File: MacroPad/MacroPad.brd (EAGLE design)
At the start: 120.6 x 68.2 mm, 69 parts, among them IC1 MIC5219BM5, J1 USB4085-GF-A_REVA4, U1 ATMEGA32U4-AUR, Y1 XRCGB16M000FXN00R0

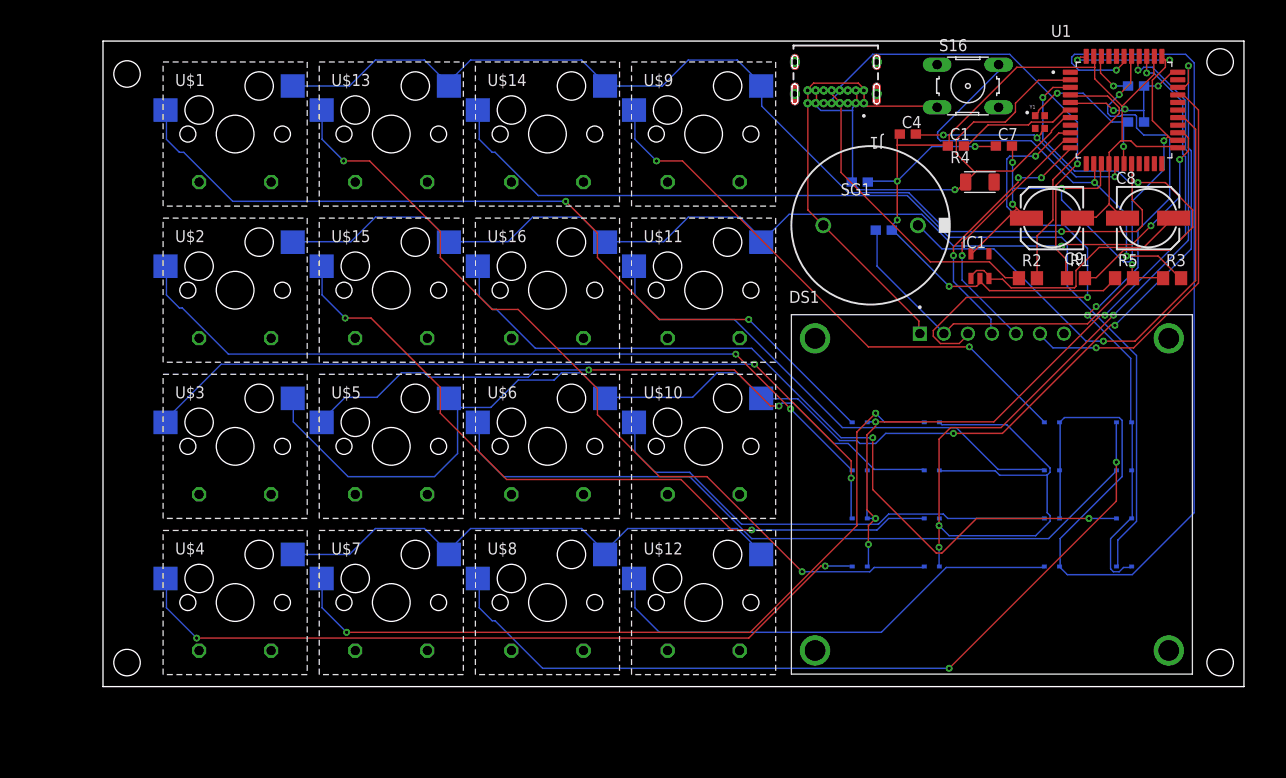
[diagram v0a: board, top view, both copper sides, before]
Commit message: Fixed some DRC errors
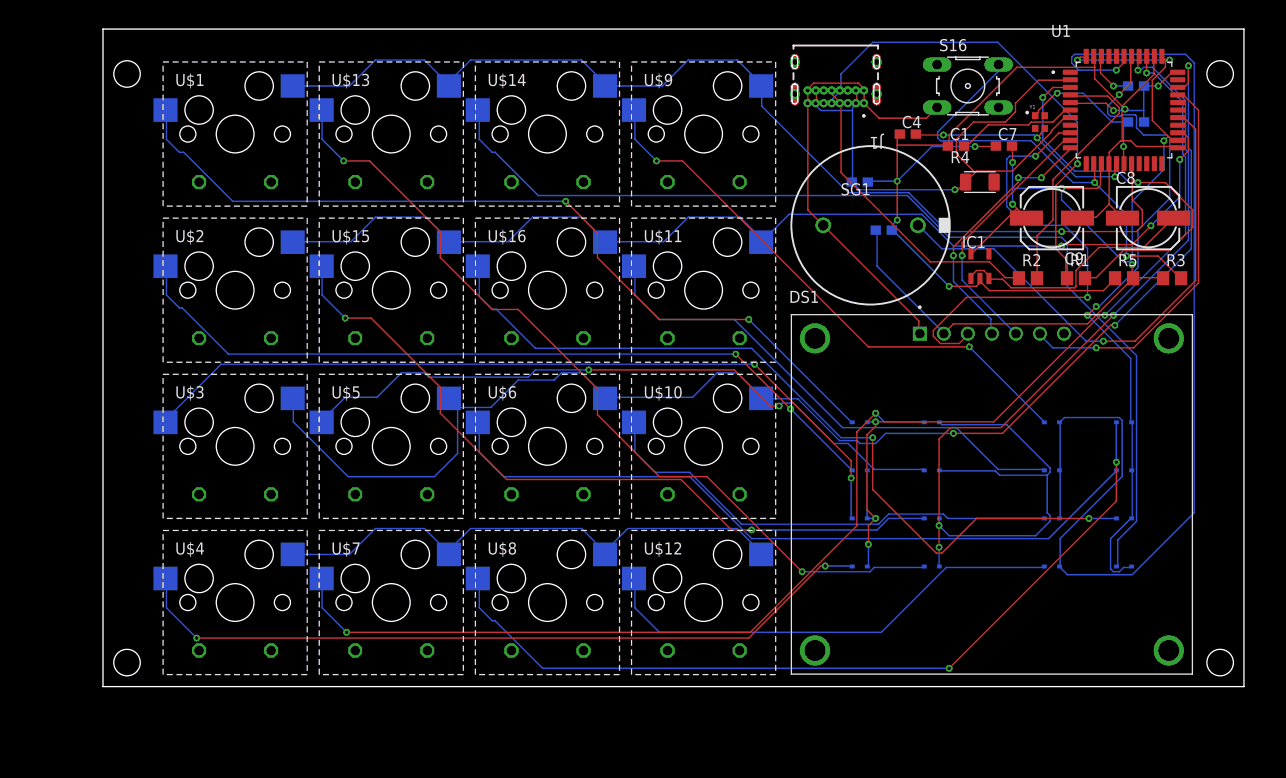
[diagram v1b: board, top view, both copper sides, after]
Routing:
- net N$20: track 49.6 -> 51.4 mm
- net DGND: track 46.8 -> 47.7 mm
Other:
- board size 120.6 x 68.2 mm -> 120.6 x 69.5 mm
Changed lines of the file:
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@@
 <drawing>
 <settings>
-<setting alwaysvectorfont="no"/>
+<setting alwaysvectorfont="yes"/>
 <setting verticaltext="up"/>
 </settings>
@@
 <plain>
 <wire x1="0" y1="0" x2="120.63" y2="0" width="0" layer="20"/>
-<wire x1="120.63" y1="0" x2="120.63" y2="68.25" width="0" layer="20"/>
-<wire x1="120.63" y1="68.25" x2="0" y2="68.25" width="0" layer="20"/>
-<wire x1="0" y1="68.25" x2="0" y2="0" width="0" layer="20"/>
+<wire x1="120.63" y1="0" x2="120.63" y2="69.52" width="0" layer="20"/>
+<wire x1="120.63" y1="69.52" x2="0" y2="69.52" width="0" layer="20"/>
+<wire x1="0" y1="69.52" x2="0" y2="0" width="0" layer="20"/>
 <hole x="2.54" y="64.77" drill="2.8"/>
 <hole x="2.54" y="2.54" drill="2.8"/>
-<hole x="118.11" y="66.04" drill="2.8"/>
+<hole x="118.11" y="64.77" drill="2.8"/>
 <hole x="118.11" y="2.54" drill="2.8"/>
 <text x="2.54" y="6.35" size="1.778" layer="45" rot="R90">Dyl's Macropad</text>
-<text x="119.38" y="21.59" size="1.778" layer="45" rot="R90">If you're reading this: have a nice day!</text>
+<text x="119.38" y="20.32" size="1.778" layer="45" rot="R90">If you're reading this: have a nice day!</text>
 </plain>
 <attributes>
@@
 <wire x1="74.5236" y1="63.0428" x2="74.495" y2="63.03" width="0.1524" layer="1"/>
 <wire x1="80.3148" y1="63.0428" x2="80.445" y2="63.03" width="0.1524" layer="1"/>
-<wire x1="80.772" y1="61.3664" x2="88.0872" y2="61.3664" width="0.1524" layer="1"/>
-<wire x1="80.4672" y1="61.6712" x2="80.772" y2="61.3664" width="0.1524" layer="1"/>
-<wire x1="88.0872" y1="61.3664" x2="88.1888" y2="61.2394" width="0.1524" layer="1"/>
+<wire x1="88.1888" y1="61.2394" x2="87.0458" y2="60.0964" width="0.1524" layer="1"/>
+<wire x1="87.0458" y1="60.0964" x2="82.042" y2="60.0964" width="0.1524" layer="1"/>
+<wire x1="80.4672" y1="61.6712" x2="82.042" y2="60.0964" width="0.1524" layer="1"/>
 <wire x1="80.4672" y1="61.6712" x2="80.445" y2="61.68" width="0.1524" layer="1"/>
 <wire x1="86.2584" y1="38.6588" x2="86.2584" y2="37.4396" width="0.1524" layer="1"/>
@@
 <wire x1="103.0224" y1="55.2704" x2="100.7364" y2="52.9844" width="0.1524" layer="1"/>
 <wire x1="103.0224" y1="59.69" x2="103.0224" y2="55.2704" width="0.1524" layer="16"/>
-<wire x1="95.8596" y1="66.8528" x2="103.0224" y2="59.69" width="0.1524" layer="16"/>
-<wire x1="81.3816" y1="66.8528" x2="95.8596" y2="66.8528" width="0.1524" layer="16"/>
-<wire x1="78.0288" y1="63.5" x2="81.3816" y2="66.8528" width="0.1524" layer="16"/>
-<wire x1="78.0288" y1="63.0428" x2="78.0288" y2="63.5" width="0.1524" layer="16"/>
+<wire x1="94.5896" y1="68.1228" x2="103.0224" y2="59.69" width="0.1524" layer="16"/>
+<wire x1="81.3816" y1="68.1228" x2="94.5896" y2="68.1228" width="0.1524" layer="16"/>
+<wire x1="78.0288" y1="64.77" x2="81.3816" y2="68.1228" width="0.1524" layer="16"/>
+<wire x1="78.0288" y1="63.0428" x2="78.0288" y2="64.77" width="0.1524" layer="16"/>
 <wire x1="101.8032" y1="43.2308" x2="101.92" y2="43.18" width="0.1524" layer="1"/>
 <wire x1="78.0288" y1="63.0428" x2="77.895" y2="63.03" width="0.1524" layer="16"/>

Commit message: Problematic DRC issues cleared
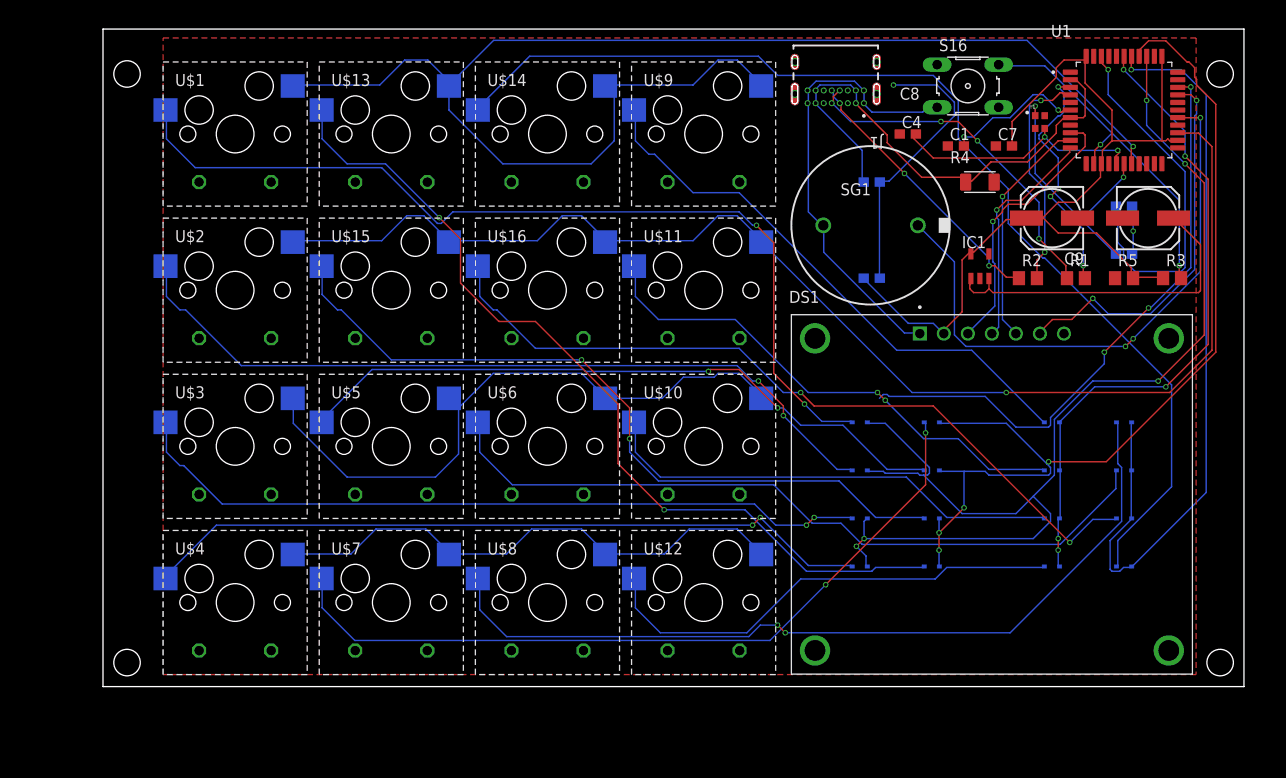
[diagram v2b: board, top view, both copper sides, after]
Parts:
- moved C5 14.0 mm to (108.0, 45.7)
- moved C2 12.8 mm to (108.0, 50.8)
- moved C6 5.24 mm to (81.3, 43.2)
- moved C3 1.27 mm to (81.3, 53.3)
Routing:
- net GND: track 131.7 -> 34.9 mm, vias 7 -> 2
- net A3: track 121.2 -> 68.8 mm, vias 1 -> 5
- net D3: track 112.5 -> 149.4 mm
- net A0: track 85.3 -> 120.6 mm
- net N$23: track 5.28 -> 39.3 mm
- net D4: track 113.8 -> 138.7 mm, vias 3 -> 1
- net D15: track 51.3 -> 29.1 mm, vias 2 -> 1
- net DN: track 42.2 -> 25.7 mm, vias 2 -> 4
- net VCC: track 116.9 -> 100.6 mm, vias 7 -> 0
- net A1: track 116.4 -> 100.9 mm
- net D5: track 146.6 -> 132.0 mm
- net N$20: track 51.4 -> 37.2 mm, vias 1 -> 3
- net A2: track 70.5 -> 82.7 mm, vias 3 -> 1
- net XTAL1: track 16.6 -> 28.0 mm
- net RST: track 47.0 -> 37.5 mm
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- added copper zone on layer 1, net GND

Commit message: Added missing diode
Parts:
- added D17: 1N4148WT, 1N4148WT:SODFL1608X70N
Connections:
- net N$17: now also D17.A
- net N$25: now also D17.C
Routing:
- net N$25: track 36.1 -> 58.3 mm
- net D5: track 132.0 -> 144.2 mm
- net N$17: track 0.00 -> 4.64 mm
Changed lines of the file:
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@@
 </layers>
 <board>
+<fusionsync huburn="a.cGVyc29uYWw6dWUyYjY3NjEz" projecturn="a.cGVyc29uYWw6dWUyYjY3NjEzIzIwMjIxMTI3NTgzMzI5MTMx" f3durn="urn:adsk.wipprod:dm.lineage:TDbepWYGSzWkHf_6D1XjyQ" pcbguid="" lastpulledtime="" lastsyncedchangeguid="" latestrevisionid="" lastsyncedrevisionid="" lastboardhashguid="" lastpushedtime="" linktopcb3d="true"/>
 <plain>
 <wire x1="0" y1="0" x2="120.63" y2="0" width="0" layer="20"/>
@@
 <attribute name="VALUE" x="82.495" y="59.725" size="1.27" layer="27" ratio="13" rot="SR180"/>
 </element>
+<element name="D17" library="1N4148WT" package="SODFL1608X70N" value="1N4148WT" x="91.44" y="49.53" smashed="yes">
+<attribute name="AVAILABILITY" value="In Stock" x="91.44" y="49.53" size="1.778" layer="27" display="off"/>
+<attribute name="DESCRIPTION" value=" Diode Standard 75 V 200mA Surface Mount SOD-523F " x="91.44" y="49.53" size="1.778" layer="27" display="off"/>
+<attribute name="MF" value="ON Semiconductor" x="91.44" y="49.53" size="1.778" layer="27" display="off"/>
+<attribute name="MP" value="1N4148WT" x="91.44" y="49.53" size="1.778" layer="27" display="off"/>
+<attribute name="NAME" x="89.99295" y="50.5116" size="0.8128" layer="25"/>
+<attribute name="PACKAGE" value="SOD-523-2 ON Semiconductor" x="91.44" y="49.53" size="1.778" layer="27" display="off"/>
+<attribute name="PRICE" value="None" x="91.44" y="49.53" size="1.778" layer="27" display="off"/>
+<attribute name="PURCHASE-URL" value="https://pricing.snapeda.com/search/part/1N4148WT/?ref=eda" x="91.44" y="49.53" size="1.778" layer="27" display="off"/>
+<attribute name="VALUE" x="89.968959375" y="47.93421875" size="0.8128" layer="27"/>
+</element>
 </elements>
 <signals>
@@
 <via x="108.9152" y="48.1584" extent="1-16" drill="0.35"/>
 <via x="83.566" y="63.6016" extent="1-16" drill="0.35"/>
+<wire x1="102.27" y1="61.76" x2="106.35" y2="55.28" width="0" layer="19" extent="1-1"/>
 </signal>
 <signal name="N$22">
@@
 <wire x1="113.3856" y1="49.3776" x2="116.0272" y2="46.736" width="0.1524" layer="1"/>
 <wire x1="113.3856" y1="49.3776" x2="113.19" y2="49.53" width="0.1524" layer="1"/>
+<contactref element="D17" pad="C"/>
+<wire x1="90.6272" y1="45.5168" x2="90.6272" y2="49.3776" width="0.1524" layer="1"/>
+<wire x1="87.7824" y1="42.672" x2="90.6272" y2="45.5168" width="0.1524" layer="1"/>
+<wire x1="87.7824" y1="36.9824" x2="87.7824" y2="42.672" width="0.1524" layer="1"/>
+<wire x1="88.5952" y1="36.1696" x2="87.7824" y2="36.9824" width="0.1524" layer="1"/>
+<wire x1="89.2048" y1="36.1696" x2="88.5952" y2="36.1696" width="0.1524" layer="1"/>
+<wire x1="90.424" y1="37.3888" x2="89.2048" y2="36.1696" width="0.1524" layer="1"/>
+<wire x1="90.424" y1="38.608" x2="90.424" y2="37.3888" width="0.1524" layer="1"/>
+<wire x1="92.0496" y1="40.2336" x2="90.424" y2="38.608" width="0.1524" layer="1"/>
+<wire x1="92.0496" y1="41.656" x2="92.0496" y2="40.2336" width="0.1524" layer="1"/>
+<wire x1="90.6272" y1="49.3776" x2="90.64" y2="49.53" width="0.1524" layer="1"/>
 </signal>
 <signal name="D2">
@@
 <wire x1="82.4992" y1="30.8864" x2="82.9056" y2="30.8864" width="0.1524" layer="16"/>
 <wire x1="82.0928" y1="30.48" x2="82.4992" y2="30.8864" width="0.1524" layer="16"/>
-<wire x1="69.59" y1="30.48" x2="69.9008" y2="30.48" width="0.1524" layer="16"/>
 <wire x1="113.792" y1="63.3984" x2="113.63" y2="63.36" width="0.1524" layer="1"/>
 <wire x1="59.1312" y1="30.48" x2="53.08" y2="30.48" width="0.1524" layer="16"/>
@@
 <via x="110.5408" y="40.0304" extent="1-16" drill="0.35"/>
 <via x="105.8672" y="35.3568" extent="1-16" drill="0.35"/>
-<wire x1="69.59" y1="30.48" x2="82.0928" y2="30.48" width="0" layer="19" extent="16-16"/>
+<wire x1="82.0928" y1="30.48" x2="69.9008" y2="30.48" width="0.1524" layer="16"/>
+<wire x1="69.9008" y1="30.48" x2="69.59" y2="30.48" width="0.1524" layer="16"/>
 </signal>
 <signal name="N$17">
 <contactref element="R4" pad="2"/>
+<contactref element="D17" pad="A"/>
+<wire x1="92.2528" y1="51.4096" x2="92.2528" y2="49.5808" width="0.1524" layer="1"/>
+<wire x1="94.0816" y1="53.2384" x2="92.2528" y2="51.4096" width="0.1524" layer="1"/>
+<wire x1="92.2528" y1="49.5808" x2="92.24" y2="49.53" width="0.1524" layer="1"/>
+<wire x1="94.0816" y1="53.2384" x2="94.215" y2="53.34" width="0.1524" layer="1"/>
 </signal>
 <signal name="D16">
@@
 </note>
 <note version="8.3" severity="warning">
+Since Version 8.3, EAGLE supports Fusion synchronisation.
+This feature will not be available in this version and saving
+the document will break the link to the Fusion PCB feature.
+</note>
+<note version="8.3" severity="warning">

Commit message: Further board errors corrected, BOM included
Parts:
- removed SG1: EFBAA40D101, buzzer:EFBAA40D101
- added U$17: PT-1307, PT-1307:PT-1307
- moved R4 21.6 mm to (78.7, 36.8)
- moved U$4 10.8 mm to (6.35, 1.27)
- moved S5 10.8 mm to (5.71, 5.08), turned to 180 degrees
- moved IC1 9.16 mm to (87.6, 36.8)
- moved S2 9.16 mm to (5.71, 24.1), turned to 180 degrees
- moved U$7 9.16 mm to (25.4, 1.27)
- moved U$3 9.16 mm to (6.35, 20.3)
- moved S7 9.16 mm to (24.8, 5.08), turned to 180 degrees
- moved C1 8.98 mm to (91.4, 48.3)
- moved D10 8.52 mm to (104.1, 15.2)
- moved D11 8.52 mm to (104.1, 10.2)
- moved D12 8.52 mm to (104.1, 5.08)
- moved D13 8.52 mm to (111.8, 20.3)
- moved D14 8.52 mm to (111.8, 15.2)
- moved D15 8.52 mm to (111.8, 10.2)
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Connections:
- net D7: now also U$17.P$2; no longer SG1.2
- net DGND: now also U$17.P$1; no longer SG1.1
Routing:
- net N$21: track 29.2 -> 68.6 mm
- net N$5: track 92.3 -> 131.2 mm
- net A0: track 120.6 -> 82.6 mm, vias 5 -> 1
- net N$2: track 83.9 -> 119.9 mm
- net GND: track 34.9 -> 0.00 mm, vias 2 -> 17
- net D6: track 56.8 -> 91.0 mm
- net N$20: track 37.2 -> 70.3 mm
- net N$13: track 59.0 -> 91.4 mm, vias 0 -> 2
- net N$3: track 79.3 -> 111.6 mm
- net N$6: track 79.2 -> 111.3 mm
- net D5: track 144.2 -> 174.2 mm, vias 3 -> 1
- net D4: track 138.7 -> 168.1 mm
- net N$10: track 82.5 -> 111.8 mm, vias 2 -> 4
- net VCC: track 100.6 -> 127.8 mm, vias 0 -> 4
- net N$1: track 97.2 -> 124.2 mm
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- added copper zone on layer 16, net GND
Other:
- board size 120.6 x 69.5 mm -> 129.5 x 77.1 mm
- board text added: "A modest macropad."
- board text added: "https://github.com/dylanmas/"
- board text removed: "Dyl's Macropad"
- board text removed: "If you're reading this: have a nice day!"
